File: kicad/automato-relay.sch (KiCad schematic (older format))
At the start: 34 parts, among them J1 TE-3-213598-4, J2 Screw_Terminal_01x03, J3 TE-3-213598-4, J4 Screw_Terminal_01x05, J5 TE-3-213598-4, J6 TE-3-213598-4, J7 Screw_Terminal_01x05, J8 TE-3-213598-4, K1 G5LE-14, K2 G5LE-14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

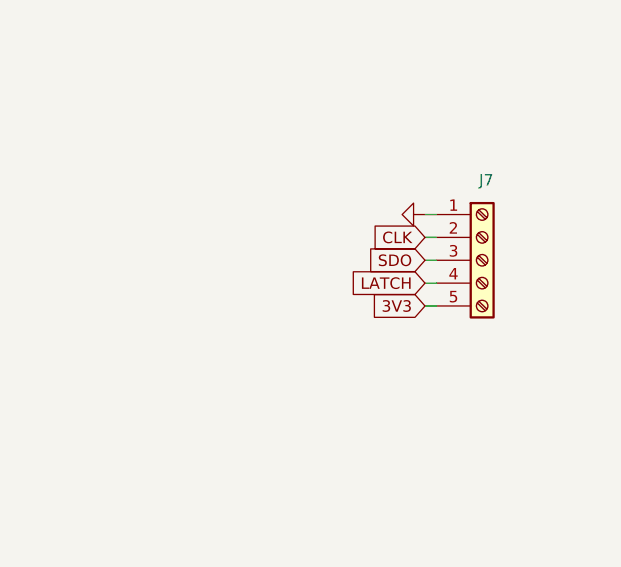
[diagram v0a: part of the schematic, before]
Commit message: remove 3V3 from J7
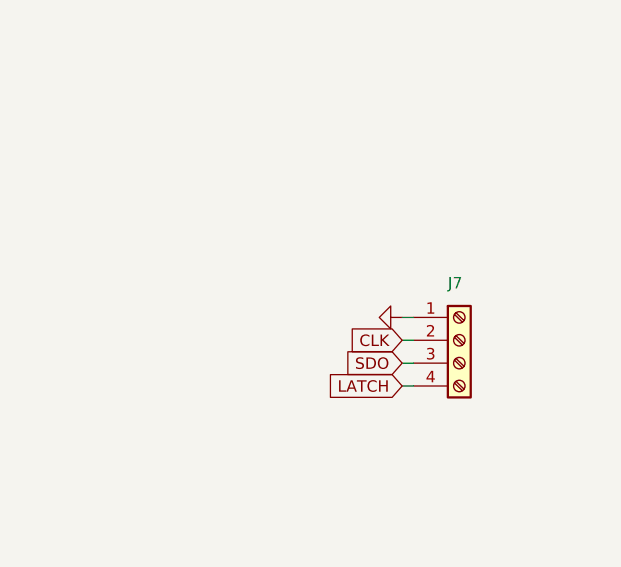
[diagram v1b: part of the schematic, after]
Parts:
- removed J7: Screw_Terminal_01x05, symbol Connector:Screw_Terminal_01x05
- added J7: Screw_Terminal_01x04, symbol Connector:Screw_Terminal_01x04
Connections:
- net CLK: now also J7.2 (Pin_2)
- net GND: now also J7.1 (Pin_1)
- net LATCH: now also J7.4 (Pin_4)
- net SDO: now also J7.3 (Pin_3)
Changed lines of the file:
@@
 L power:GND #PWR012
 U 1 1 60208E2A
-P 12050 1900
-F 0 "#PWR012" H 12050 1650 50  0001 C CNN
-F 1 "GND" H 12055 1727 50  0001 C CNN
-F 2 "" H 12050 1900 50  0001 C CNN
-F 3 "" H 12050 1900 50  0001 C CNN
-	1    12050 1900
+P 11950 2350
+F 0 "#PWR012" H 11950 2100 50  0001 C CNN
+F 1 "GND" H 11955 2177 50  0001 C CNN
+F 2 "" H 11950 2350 50  0001 C CNN
+F 3 "" H 11950 2350 50  0001 C CNN
+	1    11950 2350
 	0    1    1    0
 $EndComp
@@
 Text GLabel 6700 1300 3    50   Input ~ 0
 LATCH
-Text GLabel 12050 2000 0    50   Input ~ 0
+Text GLabel 11950 2450 0    50   Input ~ 0
 CLK
-Text GLabel 12050 2200 0    50   Input ~ 0
+Text GLabel 11950 2650 0    50   Input ~ 0
 LATCH
 Wire Wire Line
-	12100 2200 12050 2200
-Wire Wire Line
-	12050 2000 12100 2000
-Wire Wire Line
-	12050 1900 12100 1900
+	12000 2650 11950 2650
+Wire Wire Line
+	11950 2450 12000 2450
+Wire Wire Line
+	11950 2350 12000 2350
 Text GLabel 9200 2600 2    50   Input ~ 0
 SDO
 Wire Wire Line
 	9150 2600 9200 2600
-Text GLabel 12050 2100 0    50   Input ~ 0
+Text GLabel 11950 2550 0    50   Input ~ 0
 SDO
 Wire Wire Line
-	12100 2100 12050 2100
+	12000 2550 11950 2550
 $Comp
 L Connector:Screw_Terminal_01x05 J4
@@
 	8750 1450 8750 1500
 $Comp
-L Connector:Screw_Terminal_01x05 J7
-U 1 1 6023CC7C
-P 12300 2100
-F 0 "J7" H 12350 2450 50  0000 R CNN
-F 1 "Screw_Terminal_01x05" H 13400 2250 50  0001 R CNN
-F 2 "" H 12300 2100 50  0001 C CNN
-F 3 "~" H 12300 2100 50  0001 C CNN
-	1    12300 2100
-	1    0    0    -1
-$EndComp
-Text GLabel 12050 2300 0    50   Input ~ 0
-3V3
-Wire Wire Line
-	12100 2300 12050 2300
-$Comp
 L Converter_ACDC:HLK-PM03 PS1
 U 1 1 602425FA
@@
 Wire Wire Line
 	8300 2350 8300 2300
+$Comp
+L Connector:Screw_Terminal_01x04 J7
+U 1 1 60283F9B
+P 12200 2450
+F 0 "J7" H 12150 2700 50  0000 L CNN
+F 1 "Screw_Terminal_01x04" H 12280 2351 50  0001 L CNN
+F 2 "" H 12200 2450 50  0001 C CNN
+F 3 "~" H 12200 2450 50  0001 C CNN
+	1    12200 2450
+	1    0    0    -1
+$EndComp
 $EndSCHEMATC

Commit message: All traces routed
MOV added, 10 hours in.  Final approval of layout.  Power planes to pour.
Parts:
- removed J7: Screw_Terminal_01x04, symbol Connector:Screw_Terminal_01x04
- removed R1, R3, R6, R8: 240k, symbol Device:R
- added C1, C2, C3, C4: 100n, Capacitor_SMD:C_1206_3216Metric, symbol Device:C_Small
- added D10, D11, D12, D9: D, Diode_SMD:D_SOT-23_ANK, symbol Device:D
- added J7: Screw_Terminal_01x05, Connector_Phoenix_MC_HighVoltage:PhoenixContact_MC_1,5_5-G-5.08_1x05_P5.08mm_Horizontal, symbol Connector:Screw_Terminal_01x05
- added V1: Varistor, Varistor:RV_Disc_D7mm_W3.5mm_P5mm, symbol Device:Varistor
- D1, D3, D5, D7: footprint (none) -> Diode_SMD:D_SOT-23_ANK
- D2, D4, D6, D8: footprint (none) -> LED_SMD:LED_1206_3216Metric
- J1, J3, J5, J6, J8: footprint (none) -> automato-relay:TE-3-213598-4
- J2: footprint (none) -> Connector_Phoenix_MC_HighVoltage:PhoenixContact_MCV_1,5_3-G-5.08_1x03_P5.08mm_Vertical
- J4: footprint (none) -> Connector_Phoenix_MC_HighVoltage:PhoenixContact_MC_1,5_5-G-5.08_1x05_P5.08mm_Horizontal
- R2, R4, R5, R7: footprint (none) -> Resistor_SMD:R_0805_2012Metric
- U1: footprint (none) -> Package_SO:SO-16_3.9x9.9mm_P1.27mm
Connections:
- net 3V3: now also D10.1 (K), D11.1 (K), D12.1 (K), D9.1 (K)
- net ACL: now also V1.1
- net ACN: now also V1.2
- net CLK: now also J7.4 (Pin_4)
- net GND: now also J7.5 (Pin_5)
- net LATCH: now also J7.2 (Pin_2)
- net SDO: now also J7.3 (Pin_3)
- net at J1.2 (Hot), K1.1: now also C1.1
- net at K1.2, Q1.3 (D): now also D9.2 (A)
- net at D1.1 (K), D2.2 (A): now also C1.2
- net at J3.2 (Hot), K2.1: now also C2.1
- net at K2.2, Q2.3 (D): now also D10.2 (A)
- net at D3.1 (K), D4.2 (A): now also C2.2
- net at J5.2 (Hot), K3.1: now also C3.1
- net at K3.2, Q3.3 (D): now also D11.2 (A)
- net at D5.1 (K), D6.2 (A): now also C3.2
- net at J8.2 (Hot), K4.1: now also C4.1
- net at K4.2, Q4.3 (D): now also D12.2 (A)
- net at D7.1 (K), D8.2 (A): now also C4.2
